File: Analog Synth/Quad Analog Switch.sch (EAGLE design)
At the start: 17 parts, among them IC1 TL084P, Q1 J310, Q2 2N3906, T1 2N3904, T3 2N3904

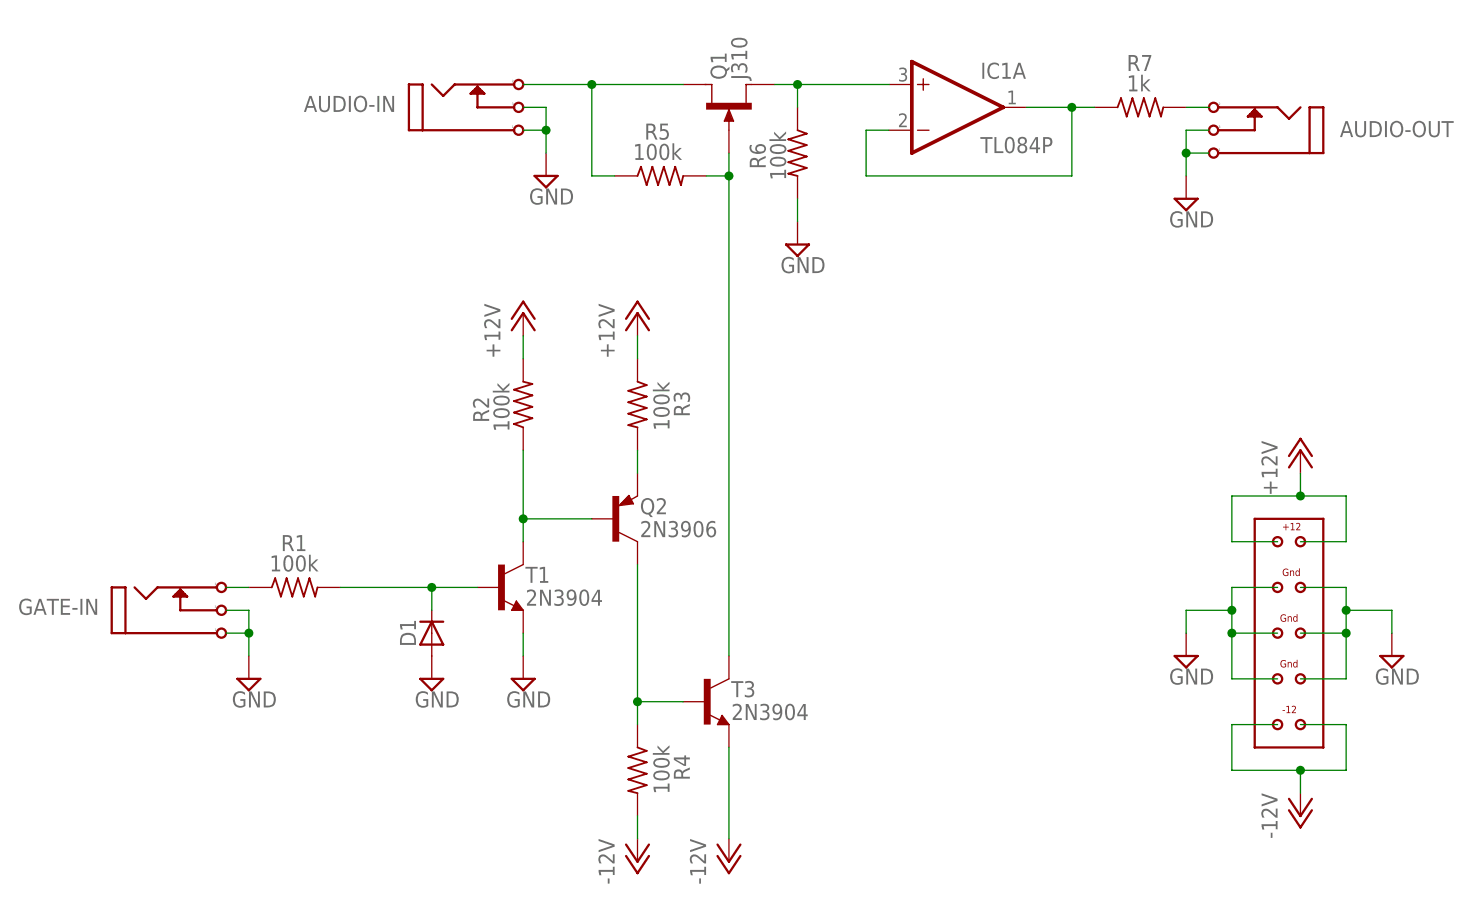
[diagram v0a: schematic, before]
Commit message: revamped the analog switch circuit. two op amps, two transistors (a diode, and some resistors)
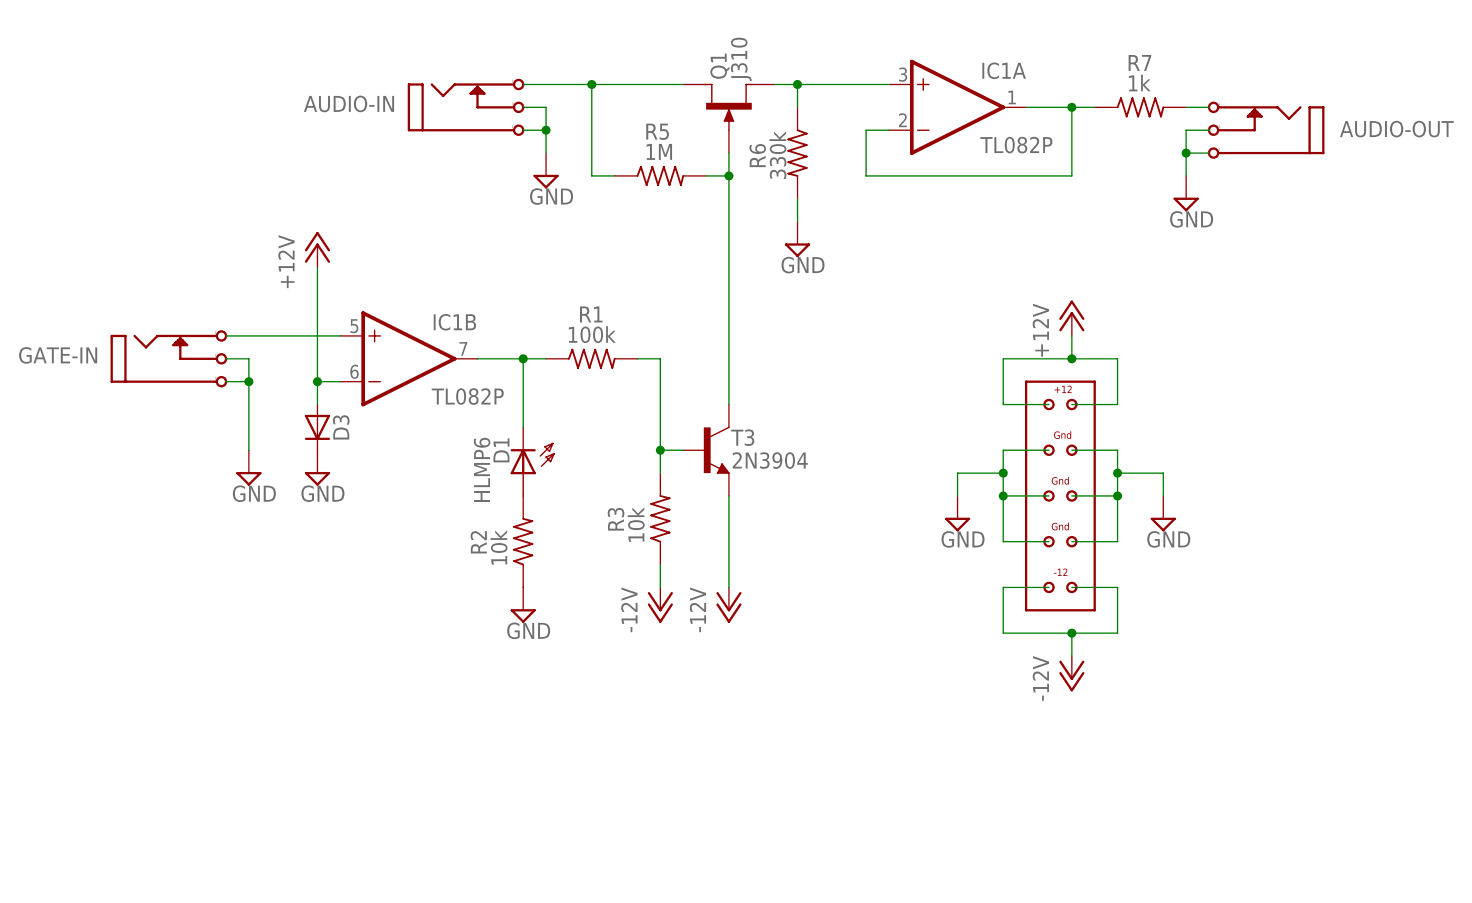
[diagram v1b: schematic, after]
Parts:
- removed Q2: 2N3906, transistor-pnp:2N3906
- removed R4: 100k, resistor:R-US_0204/2V
- removed T1: 2N3904, transistor:2N3904
- added D3: 1N4004, diode:1N4004
- D1: value 1N4004 -> HLMP6; device diode:1N4004 -> display-hp:HLMP6
- IC1: value TL084P -> TL082P; device linear:TL084P -> linear:TL082P
- R2, R3: value 100k -> 10k
- R5: value 100k -> 1M
- R6: value 100k -> 330k
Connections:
- removed net N$8: Q2.E, R3.2
- net +12V: now also D3.A, IC1B.-IN; no longer R2.2, R3.1
- net -12V: now also R3.1; no longer R4.2
- net GND: now also D3.C, R2.1; no longer D1.A, T1.E
- net N$2: now also D1.K, IC1B.OUT; no longer GATE-IN.P2
- net N$4: now also GATE-IN.P2, IC1B.+IN; no longer D1.C, R1.2, T1.B
- net N$5: now also D1.A, R2.2; no longer Q2.B, R2.1, T1.C
- net N$6: now also R1.2, R3.2; no longer Q2.C, R4.1
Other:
- moved on the sheet: GATE-IN, R1, R2, R3, T3
